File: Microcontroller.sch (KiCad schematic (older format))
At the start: 6 parts, among them J13 640456-2, J14 640456-3, J15 640456-3, J16 0022232041, J17 0022232041, U11 STM32H743ZIT6

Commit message: PCB layout
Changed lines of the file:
@@
 	3580 1410 4090 1410
 NoConn ~ 3580 1510
-NoConn ~ 3580 1610
 Wire Wire Line
 	3580 1710 4090 1710
@@
 Wire Wire Line
 	6130 4640 6640 4640
-Text HLabel 6130 4740 0    50   Input ~ 0
+Text HLabel 4090 1610 2    50   Input ~ 0
 ADC3_P
-Wire Wire Line
-	6130 4740 6640 4740
 Text HLabel 6130 4840 0    50   BiDi ~ 0
 QUADSPI_BK1_IO3
@@
 Wire Wire Line
 	1780 3510 1270 3510
+NoConn ~ 6640 4740
+Wire Wire Line
+	3580 1610 4090 1610
 $EndSCHEMATC

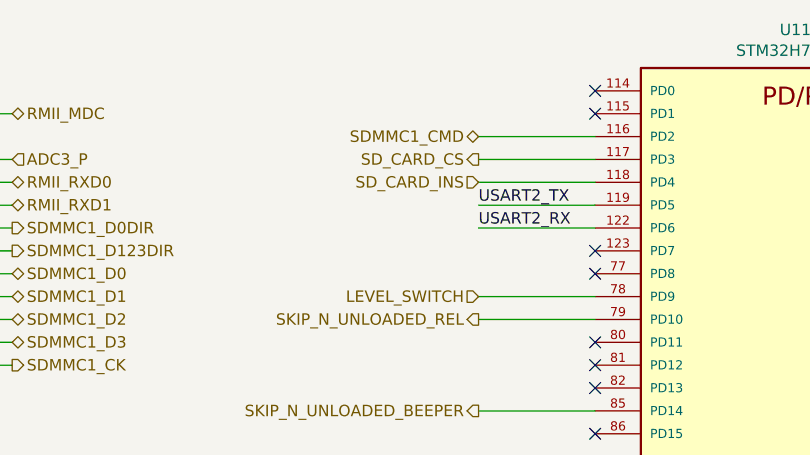
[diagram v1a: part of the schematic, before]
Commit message: Indicators layout finished
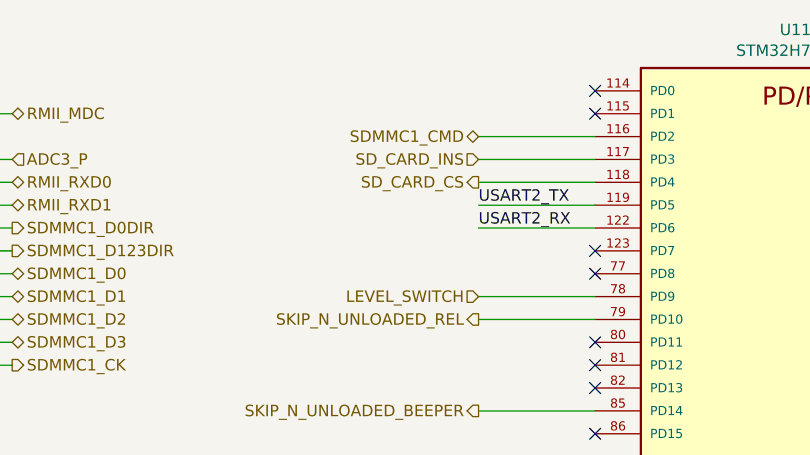
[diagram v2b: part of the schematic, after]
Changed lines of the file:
@@
 Wire Wire Line
 	1270 3910 1780 3910
-Text HLabel 6130 1710 0    50   Input ~ 0
+Text HLabel 6130 1610 0    50   Input ~ 0
 SD_CARD_INS
-Text HLabel 6130 1610 0    50   Output ~ 0
+Text HLabel 6130 1710 0    50   Output ~ 0
 SD_CARD_CS
 Wire Wire Line

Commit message: Draft PCB done
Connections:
- no-connect marks 46 -> 45
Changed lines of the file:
@@
 Text Label 1270 2710 0    50   ~ 0
 SWCLK
-NoConn ~ 1780 2810
 NoConn ~ 1780 3010
 NoConn ~ 1780 3110
@@
 Text HLabel 1270 4310 0    50   BiDi ~ 0
 RMII_TXD1
-NoConn ~ 1780 4410
-NoConn ~ 1780 4510
 Wire Wire Line
 	1270 1410 1780 1410
@@
 USART2_RX
 NoConn ~ 6640 2010
-NoConn ~ 6640 2110
-Text HLabel 6130 2210 0    50   Input ~ 0
+Text HLabel 1270 2810 0    50   Input ~ 0
 LEVEL_SWITCH
 Wire Wire Line
-	6130 2210 6640 2210
-Text HLabel 6130 2310 0    50   Output ~ 0
+	1270 2810 1780 2810
+Text HLabel 8950 1310 2    50   Output ~ 0
 SKIP_N_UNLOADED_REL
 Wire Wire Line
-	6130 2310 6640 2310
+	8950 1310 8440 1310
 NoConn ~ 6640 2410
 NoConn ~ 6640 2510
 NoConn ~ 6640 2610
-Text HLabel 6130 2710 0    50   Output ~ 0
+Text HLabel 8950 1410 2    50   Output ~ 0
 SKIP_N_UNLOADED_BEEPER
 Wire Wire Line
-	6130 2710 6640 2710
+	8440 1410 8950 1410
 NoConn ~ 6640 2810
-NoConn ~ 8440 1310
-NoConn ~ 8440 1410
 Wire Wire Line
 	8950 1510 8440 1510
@@
 Wire Wire Line
 	6640 4540 6130 4540
-Text HLabel 6130 4640 0    50   Input ~ 0
+Text HLabel 1270 4510 0    50   Input ~ 0
 A_CH3_FAULT
 Wire Wire Line
-	6130 4640 6640 4640
+	1270 4510 1780 4510
 Text HLabel 4090 1610 2    50   Input ~ 0
 ADC3_P
@@
 Wire Wire Line
 	6130 5240 6640 5240
-Text HLabel 6130 5340 0    50   Input ~ 0
+Text HLabel 6130 2110 0    50   Input ~ 0
 A_CH1_FAULT
 Wire Wire Line
-	6130 5340 6640 5340
+	6130 2110 6640 2110
 Text HLabel 6130 5440 0    50   Input ~ 0
 ADC1_P
@@
 Wire Wire Line
 	6130 5540 6640 5540
-Text HLabel 6130 5640 0    50   Input ~ 0
+Text HLabel 1270 4410 0    50   Input ~ 0
 A_CH2_FAULT
 Wire Wire Line
-	6130 5640 6640 5640
+	1270 4410 1780 4410
 NoConn ~ 6640 5740
 NoConn ~ 8440 4340
@@
 Wire Wire Line
 	8440 4640 8950 4640
+Text HLabel 8950 4940 2    50   Input ~ 0
+Button_Emh
+Wire Wire Line
+	8440 4740 8950 4740
+Text HLabel 8950 4840 2    50   Input ~ 0
+Button_Clock
+Wire Wire Line
+	8440 4840 8950 4840
+Text HLabel 8950 4740 2    50   Input ~ 0
+Button_pH
+Wire Wire Line
+	8440 4940 8950 4940
 Text HLabel 8950 4640 2    50   Input ~ 0
-Button_Emh
-Wire Wire Line
-	8440 4740 8950 4740
-Text HLabel 8950 4740 2    50   Input ~ 0
-Button_Clock
-Wire Wire Line
-	8440 4840 8950 4840
-Text HLabel 8950 4840 2    50   Input ~ 0
-Button_pH
-Wire Wire Line
-	8440 4940 8950 4940
-Text HLabel 8950 4940 2    50   Input ~ 0
 Button_Func
 Wire Wire Line
@@
 Wire Wire Line
 	3580 1610 4090 1610
+NoConn ~ 6640 2310
+NoConn ~ 6640 2210
+NoConn ~ 6640 5640
+NoConn ~ 6640 5340
+NoConn ~ 6640 4640
 $EndSCHEMATC

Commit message: PCB minor changes
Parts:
- J13: value 640456-2 -> I2C
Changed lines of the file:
@@
 P 3580 5720
 F 0 "J13" V 3460 5660 50  0000 C CNN
-F 1 "640456-2" V 3900 5740 50  0000 C CNN
+F 1 "I2C" V 3786 5666 50  0000 C CNN
 F 2 "Connector_PinHeader_2.54mm:PinHeader_1x02_P2.54mm_Vertical" H 3780 5920 60  0001 L CNN
 F 3 "https://www.te.com/commerce/DocumentDelivery/DDEController?Action=srchrtrv&DocNm=640456&DocType=Customer+Drawing&DocLang=English" H 3780 6020 60  0001 L CNN

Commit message: PCB before Gerber creating
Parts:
- removed J13: I2C, Connector_PinHeader_2.54mm:PinHeader_1x02_P2.54mm_Vertical, symbol dk_Rectangular-Connectors-Headers-Male-Pins:640456-2
- added J13: 640456-3, Connector_PinHeader_2.54mm:PinHeader_1x03_P2.54mm_Vertical, symbol dk_Rectangular-Connectors-Headers-Male-Pins:640456-3
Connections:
- wire segments 83 -> 85
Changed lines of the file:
@@
 Text Label 3160 6560 2    50   ~ 0
 SPI4_MOSI
-$Comp
-L dk_Rectangular-Connectors-Headers-Male-Pins:640456-2 J13
-U 1 1 612E235D
-P 3580 5720
-F 0 "J13" V 3460 5660 50  0000 C CNN
-F 1 "I2C" V 3786 5666 50  0000 C CNN
-F 2 "Connector_PinHeader_2.54mm:PinHeader_1x02_P2.54mm_Vertical" H 3780 5920 60  0001 L CNN
-F 3 "https://www.te.com/commerce/DocumentDelivery/DDEController?Action=srchrtrv&DocNm=640456&DocType=Customer+Drawing&DocLang=English" H 3780 6020 60  0001 L CNN
-F 4 "A1921-ND" H 3780 6120 60  0001 L CNN "Digi-Key_PN"
-F 5 "640456-2" H 3780 6220 60  0001 L CNN "MPN"
-F 6 "Connectors, Interconnects" H 3780 6320 60  0001 L CNN "Category"
-F 7 "Rectangular Connectors - Headers, Male Pins" H 3780 6420 60  0001 L CNN "Family"
-F 8 "https://www.te.com/commerce/DocumentDelivery/DDEController?Action=srchrtrv&DocNm=640456&DocType=Customer+Drawing&DocLang=English" H 3780 6520 60  0001 L CNN "DK_Datasheet_Link"
-F 9 "/product-detail/en/te-connectivity-amp-connectors/640456-2/A1921-ND/109003" H 3780 6620 60  0001 L CNN "DK_Detail_Page"
-F 10 "CONN HEADER VERT 2POS 2.54MM" H 3780 6720 60  0001 L CNN "Description"
-F 11 "TE Connectivity AMP Connectors" H 3780 6820 60  0001 L CNN "Manufacturer"
-F 12 "Active" H 3780 6920 60  0001 L CNN "Status"
-	1    3580 5720
-	0    1    1    0
-$EndComp
 Wire Wire Line
 	3680 5720 4310 5720
@@
 NoConn ~ 6640 5340
 NoConn ~ 6640 4640
+$Comp
+L dk_Rectangular-Connectors-Headers-Male-Pins:640456-3 J13
+U 1 1 60D551B2
+P 3580 5720
+F 0 "J13" V 3472 5672 50  0000 C CNN
+F 1 "640456-3" V 3898 5672 50  0000 C CNN
+F 2 "Connector_PinHeader_2.54mm:PinHeader_1x03_P2.54mm_Vertical" H 3780 5920 60  0001 L CNN
+F 3 "https://www.te.com/commerce/DocumentDelivery/DDEController?Action=srchrtrv&DocNm=640456&DocType=Customer+Drawing&DocLang=English" H 3780 6020 60  0001 L CNN
+F 4 "A19470-ND" H 3780 6120 60  0001 L CNN "Digi-Key_PN"
+F 5 "640456-3" H 3780 6220 60  0001 L CNN "MPN"
+F 6 "Connectors, Interconnects" H 3780 6320 60  0001 L CNN "Category"
+F 7 "Rectangular Connectors - Headers, Male Pins" H 3780 6420 60  0001 L CNN "Family"
+F 8 "https://www.te.com/commerce/DocumentDelivery/DDEController?Action=srchrtrv&DocNm=640456&DocType=Customer+Drawing&DocLang=English" H 3780 6520 60  0001 L CNN "DK_Datasheet_Link"
+F 9 "/product-detail/en/te-connectivity-amp-connectors/640456-3/A19470-ND/259010" H 3780 6620 60  0001 L CNN "DK_Detail_Page"
+F 10 "CONN HEADER VERT 3POS 2.54MM" H 3780 6720 60  0001 L CNN "Description"
+F 11 "TE Connectivity AMP Connectors" H 3780 6820 60  0001 L CNN "Manufacturer"
+F 12 "Active" H 3780 6920 60  0001 L CNN "Status"
+	1    3580 5720
+	0    1    1    0
+$EndComp
+$Comp
+L power:GNDREF #PWR?
+U 1 1 60D5728A
+P 3820 6070
+AR Path="/60D5728A" Ref="#PWR?"  Part="1"
+AR Path="/60A03F8A/60D5728A" Ref="#PWR?"  Part="1"
+AR Path="/60D8C564/60D5728A" Ref="#PWR?"  Part="1"
+AR Path="/60CDB738/60D5728A" Ref="#PWR0108"  Part="1"
+F 0 "#PWR0108" H 3820 5820 50  0001 C CNN
+F 1 "GNDREF" V 3825 5942 50  0001 R CNN
+F 2 "" H 3820 6070 50  0001 C CNN
+F 3 "" H 3820 6070 50  0001 C CNN
+	1    3820 6070
+	1    0    0    -1
+$EndComp
+Wire Wire Line
+	3680 5920 3820 5920
+Wire Wire Line
+	3820 5920 3820 6070
 $EndSCHEMATC

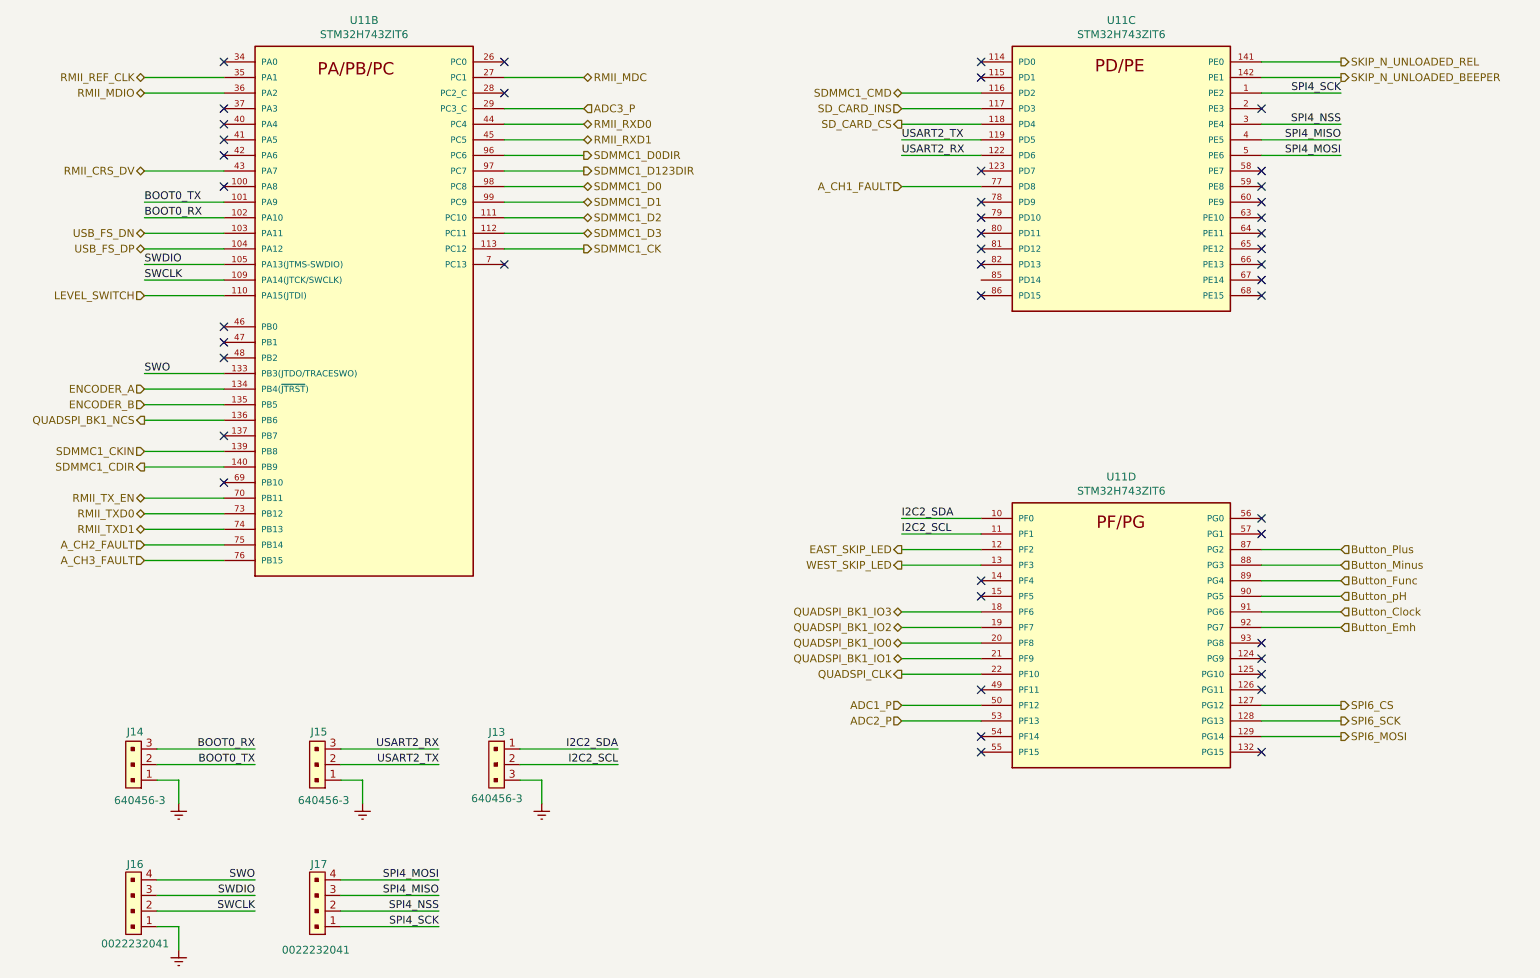
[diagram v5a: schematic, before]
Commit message: minor changes and add NRST to J16
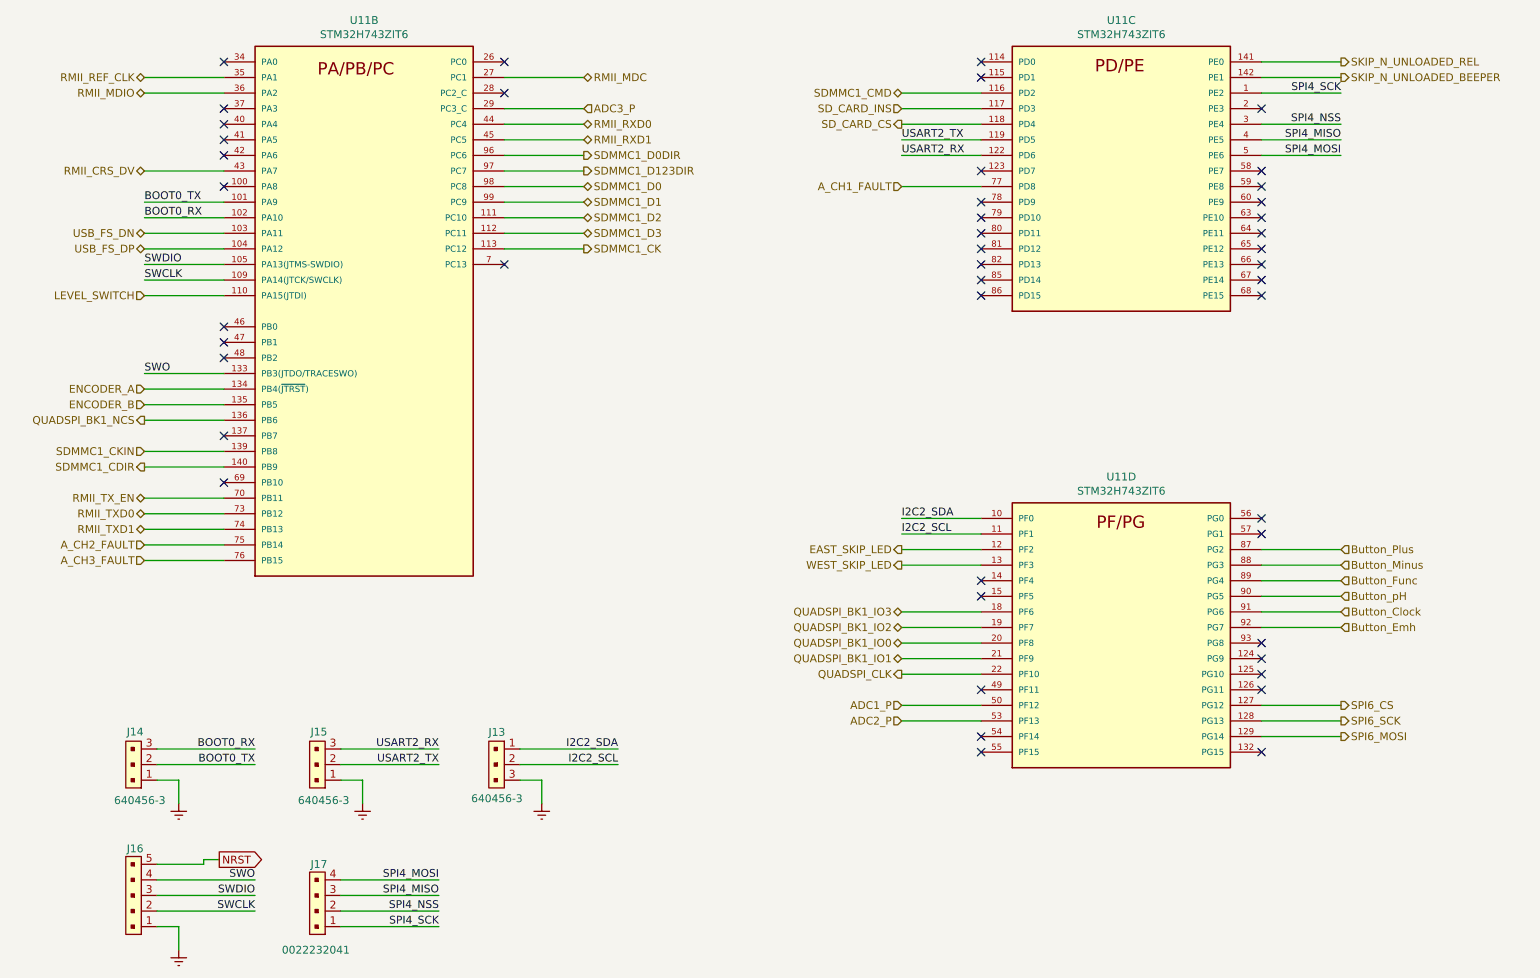
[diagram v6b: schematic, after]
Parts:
- removed J16: 0022232041, Connector_PinHeader_2.54mm:PinHeader_1x04_P2.54mm_Vertical, symbol dk_Rectangular-Connectors-Headers-Male-Pins:0022232041
- added J16: B5B-XH-A_LF__SN_, Connector_PinHeader_2.54mm:PinHeader_1x05_P2.54mm_Vertical, symbol dk_Rectangular-Connectors-Headers-Male-Pins:B5B-XH-A_LF__SN_
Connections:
- net GNDREF: now also J16.1
- net SWCLK: now also J16.2
- net SWDIO: now also J16.3
- net SWO: now also J16.4
- new net NRST: J16.5
- no-connect marks 45 -> 46
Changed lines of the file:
@@
-	0    1    -1   0
-$EndComp
-$Comp
-L dk_Rectangular-Connectors-Headers-Male-Pins:0022232041 J16
-U 1 1 612AA072
-P 1250 6860
-F 0 "J16" V 1650 6820 50  0000 C CNN
-F 1 "0022232041" V 1140 6820 50  0000 C CNN
-F 2 "Connector_PinHeader_2.54mm:PinHeader_1x04_P2.54mm_Vertical" H 1450 7060 60  0001 L CNN
-F 3 "https://www.molex.com/pdm_docs/sd/022232041_sd.pdf" H 1450 7160 60  0001 L CNN
-F 4 "WM4202-ND" H 1450 7260 60  0001 L CNN "Digi-Key_PN"
-F 5 "0022232041" H 1450 7360 60  0001 L CNN "MPN"
-F 6 "Connectors, Interconnects" H 1450 7460 60  0001 L CNN "Category"
-F 7 "Rectangular Connectors - Headers, Male Pins" H 1450 7560 60  0001 L CNN "Family"
-F 8 "https://www.molex.com/pdm_docs/sd/022232041_sd.pdf" H 1450 7660 60  0001 L CNN "DK_Datasheet_Link"
-F 9 "/product-detail/en/molex/0022232041/WM4202-ND/26671" H 1450 7760 60  0001 L CNN "DK_Detail_Page"
-F 10 "CONN HEADER VERT 4POS 2.54MM" H 1450 7860 60  0001 L CNN "Description"
-F 11 "Molex" H 1450 7960 60  0001 L CNN "Manufacturer"
-F 12 "Active" H 1450 8060 60  0001 L CNN "Status"
-	1    1250 6860
 	0    1    -1   0
 $EndComp
@@
 Wire Wire Line
 	3820 5920 3820 6070
+NoConn ~ 6640 2710
+$Comp
+L dk_Rectangular-Connectors-Headers-Male-Pins:B5B-XH-A_LF__SN_ J16
+U 1 1 60C6DEE0
+P 1250 6860
+F 0 "J16" V 1750 6820 50  0000 C CNN
+F 1 "B5B-XH-A_LF__SN_" V 1080 6900 50  0001 C CNN
+F 2 "Connector_PinHeader_2.54mm:PinHeader_1x05_P2.54mm_Vertical" H 1450 7060 60  0001 L CNN
+F 3 "http://www.jst-mfg.com/product/pdf/eng/eXH.pdf" H 1450 7160 60  0001 L CNN
+F 4 "455-2270-ND" H 1450 7260 60  0001 L CNN "Digi-Key_PN"
+F 5 "B5B-XH-A(LF)(SN)" H 1450 7360 60  0001 L CNN "MPN"
+F 6 "Connectors, Interconnects" H 1450 7460 60  0001 L CNN "Category"
+F 7 "Rectangular Connectors - Headers, Male Pins" H 1450 7560 60  0001 L CNN "Family"
+F 8 "http://www.jst-mfg.com/product/pdf/eng/eXH.pdf" H 1450 7660 60  0001 L CNN "DK_Datasheet_Link"
+F 9 "/product-detail/en/jst-sales-america-inc/B5B-XH-A(LF)(SN)/455-2270-ND/1530483" H 1450 7760 60  0001 L CNN "DK_Detail_Page"
+F 10 "CONN HEADER VERT 5POS 2.5MM" H 1450 7860 60  0001 L CNN "Description"
+F 11 "JST Sales America Inc." H 1450 7960 60  0001 L CNN "Manufacturer"
+F 12 "Active" H 1450 8060 60  0001 L CNN "Status"
+	1    1250 6860
+	0    1    -1   0
+$EndComp
+Wire Wire Line
+	1350 6460 1650 6460
+Text GLabel 1750 6430 2    50   Output ~ 0
+NRST
+Wire Wire Line
+	1650 6460 1650 6430
+Wire Wire Line
+	1650 6430 1750 6430
 $EndSCHEMATC
